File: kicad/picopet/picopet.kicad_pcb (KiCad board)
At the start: 2 copper layers, 56 parts, among them J1 USB_C_Receptacle_USB2.0_14P, J2 PH1.25mm 2P, J3 PH1.25mm 2P, J4 CR1220 Holder, J5 ST7735 LCD, Q1 SS8050, SW1 PWR, SW2 BOOTSEL, SW3 Btn0, SW4 Btn1, SW5 Btn2, SW6 Btn3, U1 RP2040, U2 MCP73831-2-OT, U3 S-T111B33MC-OGSTFU, U4 DS3231MZ, U6 AT24CS32-SSHM, U7 W25Q32JVSSIQ, Y1 X322512MSB4SI

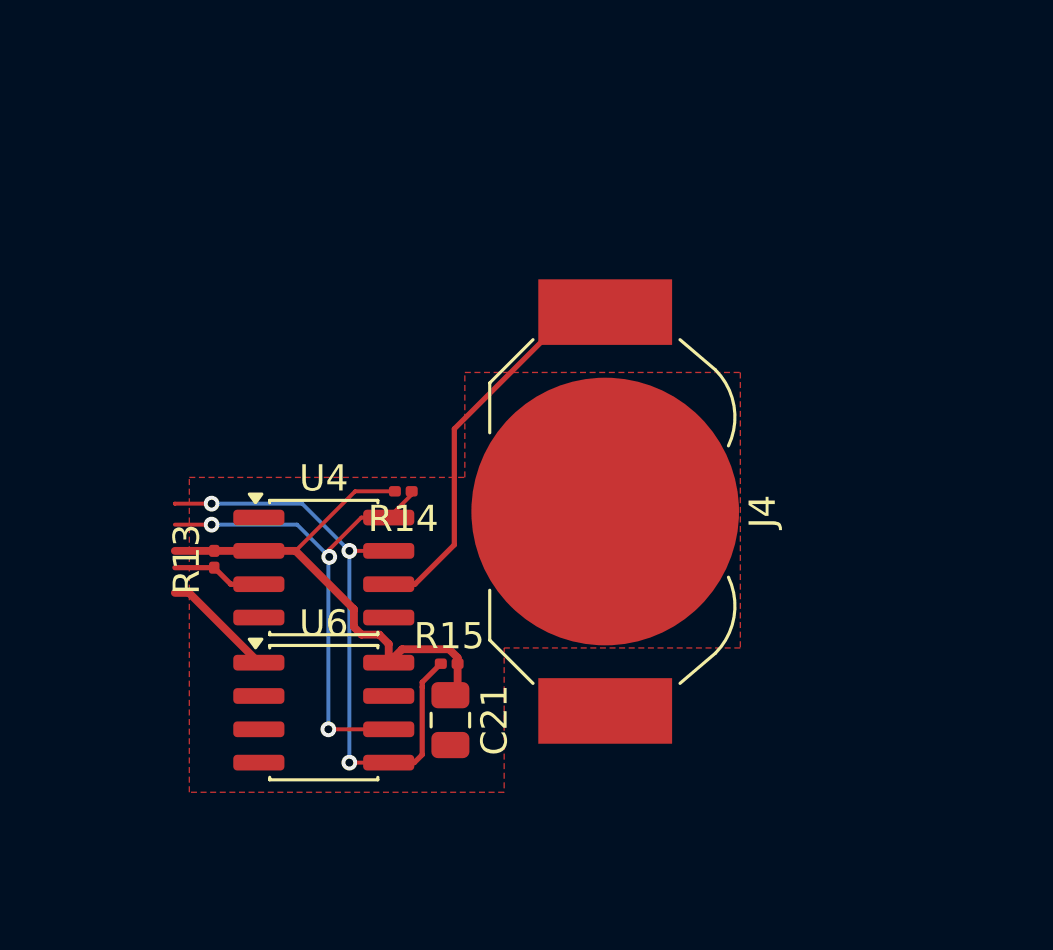
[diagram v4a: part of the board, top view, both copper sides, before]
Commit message: Considering making custom RTC module first with pcb fab
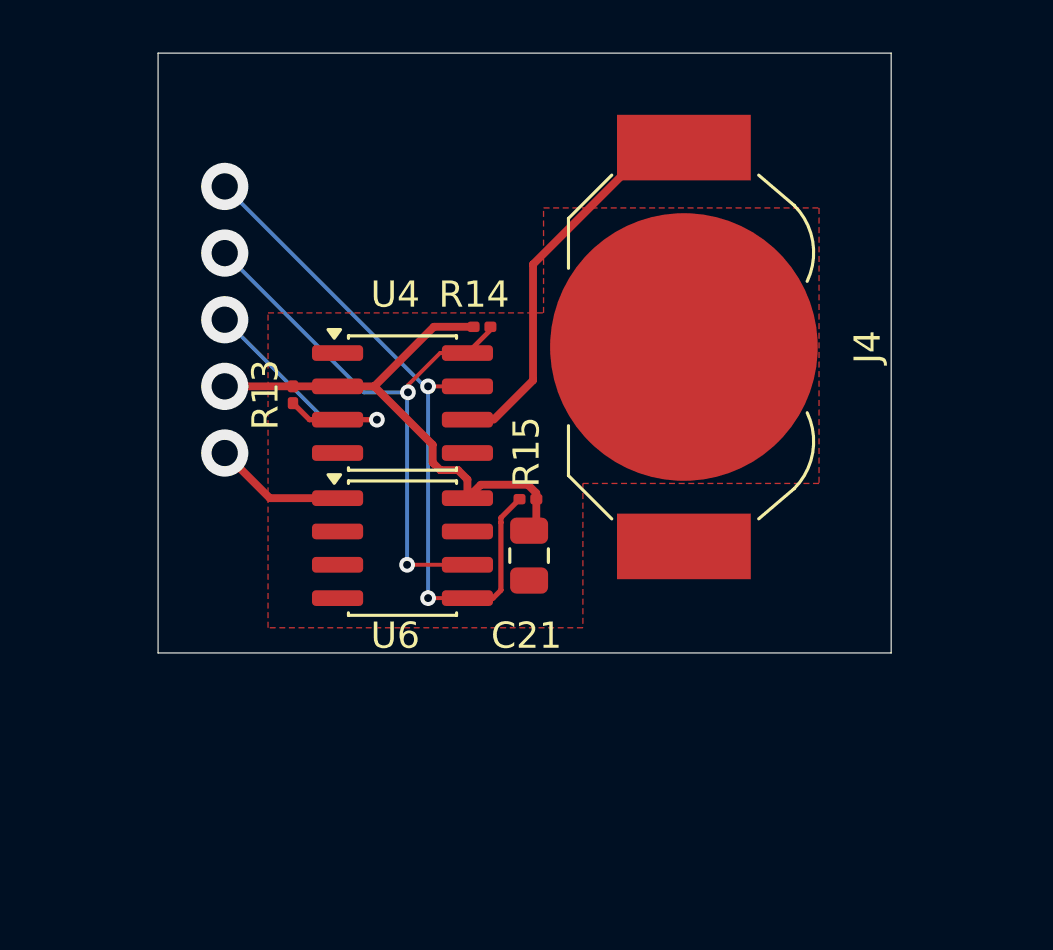
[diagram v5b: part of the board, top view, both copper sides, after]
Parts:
- moved J4 6.95 mm to (78.0, 38.0)
- moved R13 6.95 mm to (63.1, 39.8)
- moved R14 6.95 mm to (70.3, 37.2)
- moved R15 6.95 mm to (72.1, 43.8)
- moved U4 6.95 mm to (67.3, 40.1)
- moved U6 6.95 mm to (67.3, 45.7)
- moved C21 6.95 mm to (72.1, 46.0)
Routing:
- net GPIO5: track 4.36 -> 11.7 mm, vias 1 -> 3
- net GPIO0: track 25.8 -> 29.3 mm
- net GPIO1: track 22.3 -> 25.1 mm
- net +3V3: track 79.7 -> 80.8 mm, vias 9 -> 10
- net GND: track 33.4 -> 34.1 mm, vias 4 -> 5
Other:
- board outline added: 27.9 x 22.9 mm
- board text added: "3V3"
- board text added: "GND"
- board text added: "SCL"
- board text added: "SDA"
- board text added: "SQW"

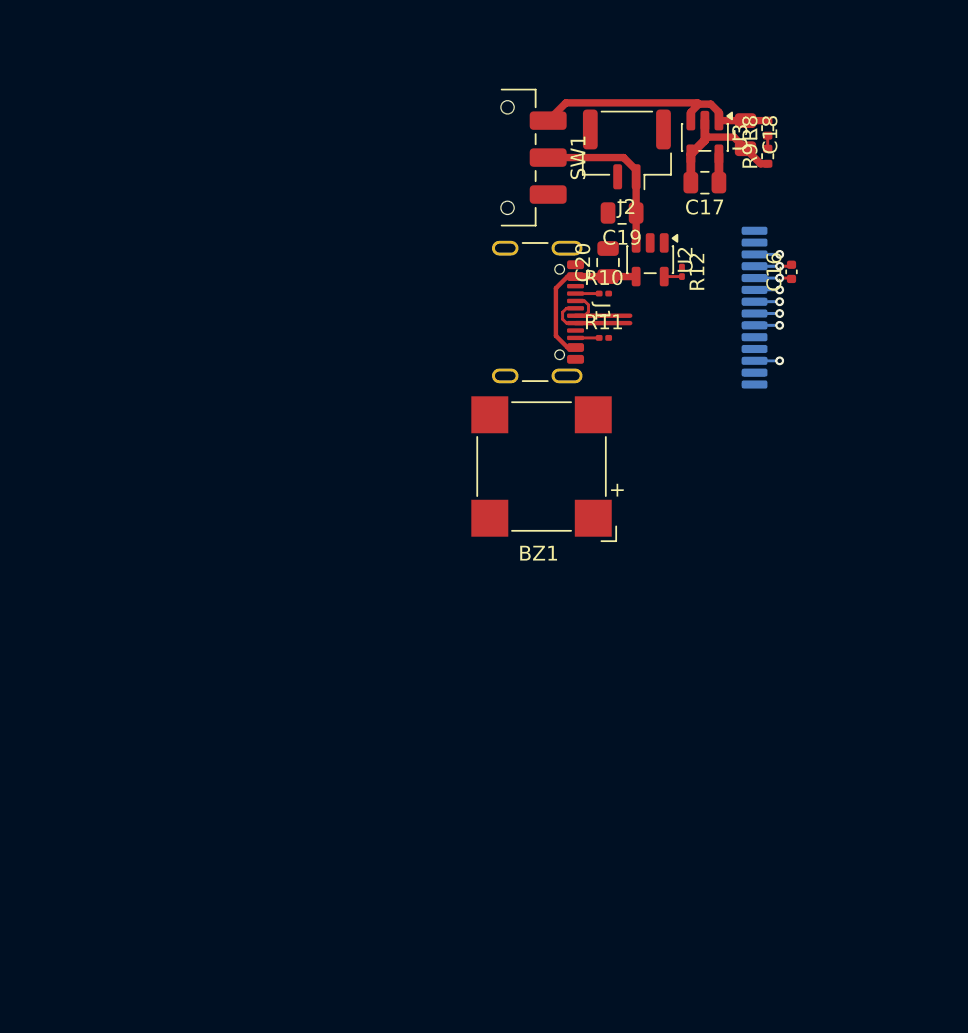
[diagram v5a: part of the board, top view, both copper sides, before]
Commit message: Separated rtc+nvm module for test fabrication
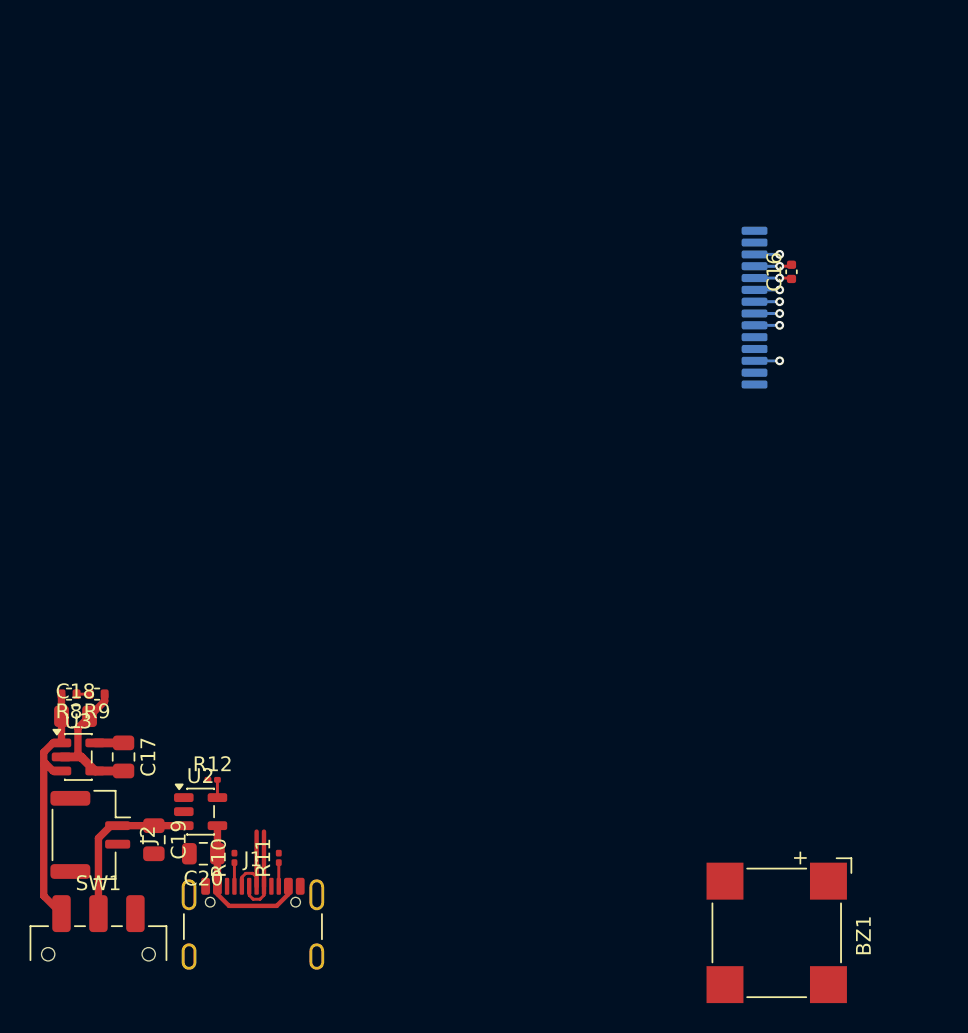
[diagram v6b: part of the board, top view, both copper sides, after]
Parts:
- moved R8 60.8 mm to (16.6, 112.3), turned to 180 degrees
- moved SW1 60.6 mm to (18.6, 129.9), turned to 0 degrees
- moved C18 60.0 mm to (17.1, 113.8), turned to 0 degrees
- moved U3 59.6 mm to (17.3, 116.6), turned to 0 degrees
- moved J2 58.9 mm to (18.1, 121.9), turned to -90 degrees
- moved R9 58.2 mm to (18.5, 112.3), turned to 180 degrees
- moved C17 55.3 mm to (20.3, 116.6), turned to -90 degrees
- moved C19 52.9 mm to (22.4, 122.2), turned to -90 degrees
- moved C20 48.5 mm to (25.7, 123.1), turned to 180 degrees
- moved U2 48.2 mm to (25.5, 120.3), turned to 0 degrees
- moved R12 46.8 mm to (26.3, 118.1), turned to 0 degrees
- moved J1 46.2 mm to (29.1, 129.0), turned to 0 degrees
- moved R10 45.6 mm to (27.8, 123.4), turned to 90 degrees
- moved R11 41.5 mm to (30.8, 123.4), turned to 90 degrees
- moved BZ1 35.3 mm to (64.5, 128.5), turned to -90 degrees

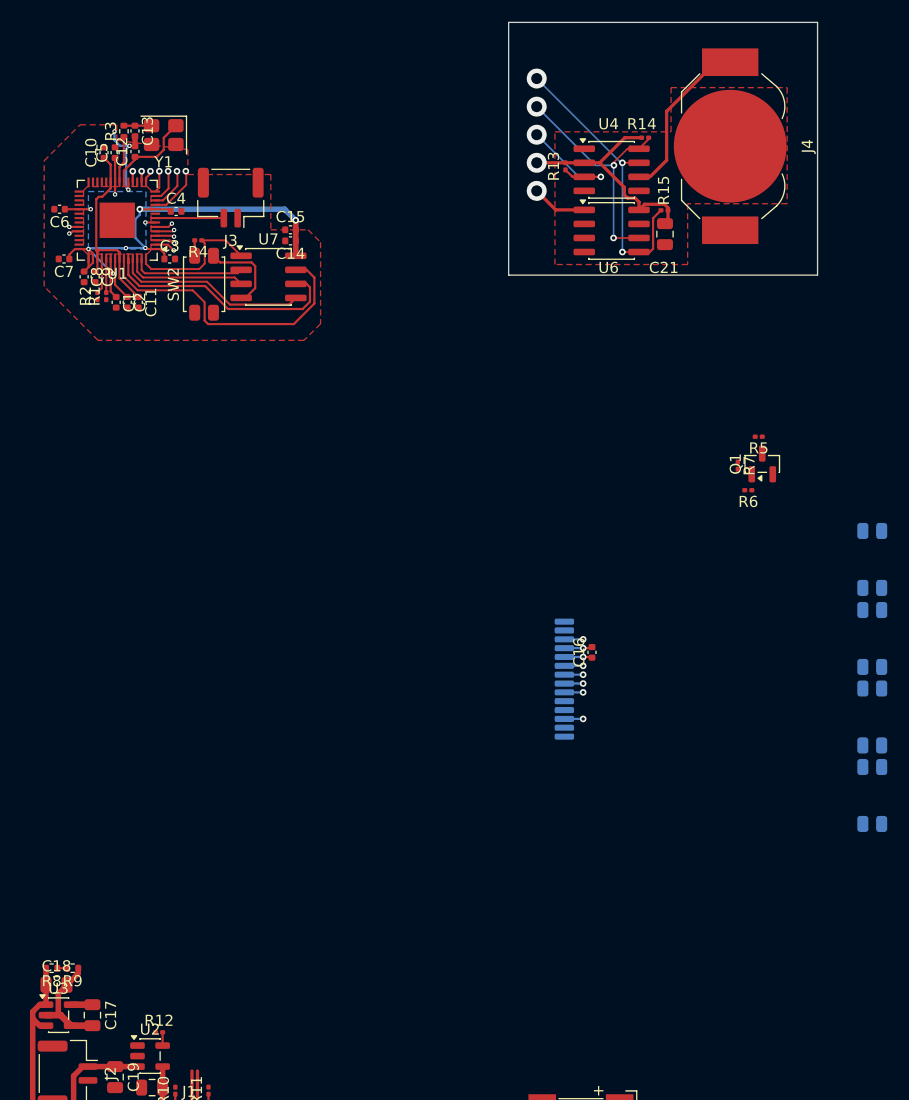
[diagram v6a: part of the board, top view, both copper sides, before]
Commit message: Updated fab files for rtc_nvm module
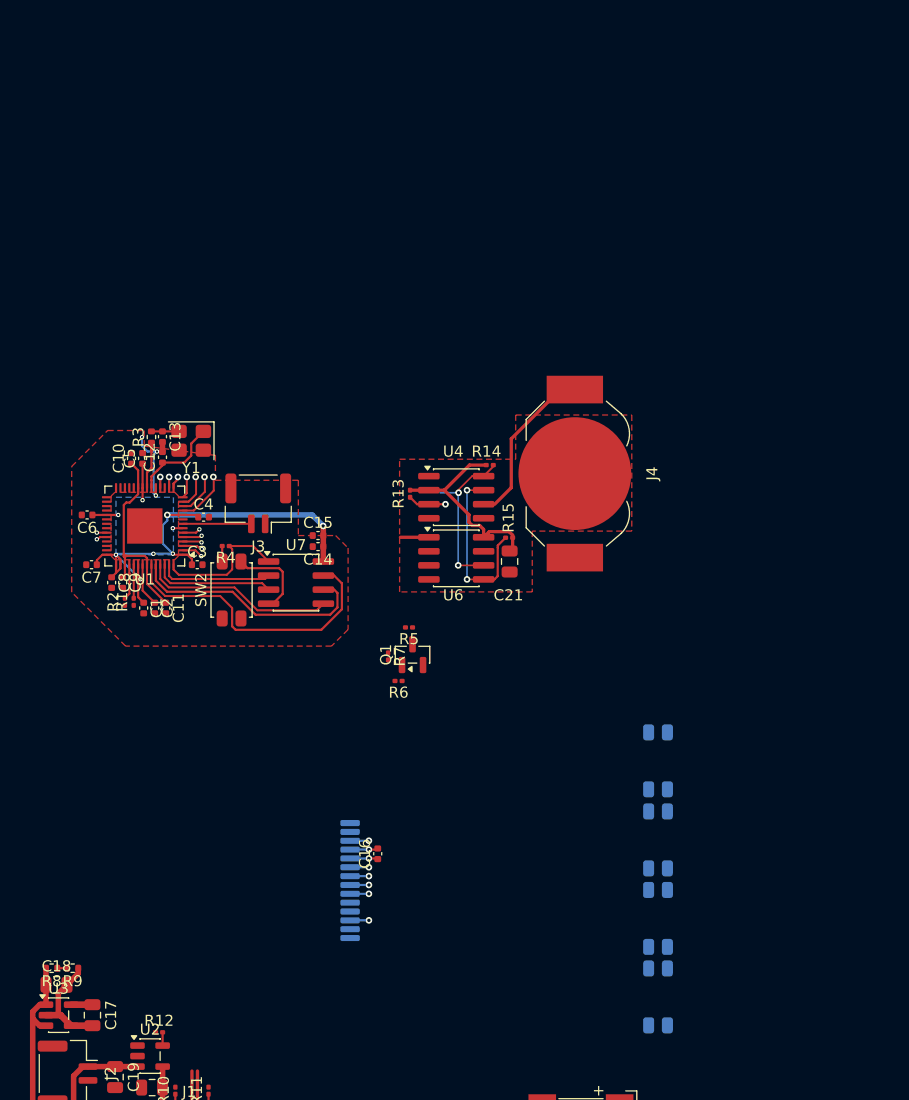
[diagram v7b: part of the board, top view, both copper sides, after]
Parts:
- moved R6 36.0 mm to (48.0, 86.4)
- moved Q1 36.0 mm to (49.3, 84.0)
- moved R5 36.0 mm to (48.9, 81.5)
- moved R7 36.0 mm to (47.1, 84.1)
- moved R14 32.8 mm to (56.3, 66.8)
- moved U4 32.8 mm to (53.2, 69.7)
- moved U6 32.8 mm to (53.2, 75.3)
- moved R13 32.8 mm to (49.0, 69.4)
- moved R15 32.8 mm to (58.0, 73.4)
- moved C21 32.8 mm to (58.0, 75.6)
- moved J4 32.8 mm to (63.9, 67.6)
- moved C12 27.8 mm to (26.6, 66.1)
- moved C13 27.8 mm to (26.6, 64.3)
- moved C14 27.8 mm to (40.7, 74.2)
- moved C15 27.8 mm to (40.7, 73.2)
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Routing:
- net GPIO0: track 29.3 -> 18.6 mm, vias 4 -> 3
- net GPIO1: track 25.1 -> 17.6 mm, vias 4 -> 3
- net GPIO5: track 11.7 -> 6.35 mm, vias 3 -> 2
- net +3V3: track 80.8 -> 78.2 mm, vias 10 -> 9
- net GND: track 34.1 -> 31.6 mm, vias 5 -> 4
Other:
- board outline removed
- board text removed: "3V3"
- board text removed: "GND"
- board text removed: "SCL"
- board text removed: "SDA"
- board text removed: "SQW"

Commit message: Various kicad edits
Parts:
- BZ1: footprint Buzzer_Beeper:MagneticBuzzer_CUI_CMT-8504-100-SMT -> Buzzer_Beeper:MagneticBuzzer_Kobitone_254-EMB84Q-RO
- moved BZ1 22.7 mm to (41.8, 128.2)
